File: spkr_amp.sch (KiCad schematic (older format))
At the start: 4 parts, among them U2 FSA2275UMX, U3 TPA2006D1DRBR

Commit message: Lots of schematic cleanup and board tweaking
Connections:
- wire segments 6 -> 11
- no-connect marks 1 -> 0
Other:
- moved on the sheet: C3, C7, U5
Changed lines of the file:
@@
 $Descr A4 11693 8268
 encoding utf-8
-Sheet 3 3
+Sheet 2 3
 Title ""
 Date ""
@@
 L TPA2006D1DRBR:TPA2006D1DRBR U?
 U 1 1 6026AF34
-P 5500 3300
+P 6900 3500
 AR Path="/6026AF34" Ref="U?"  Part="1"
 AR Path="/6026A3BE/6026AF34" Ref="U3"  Part="1"
 AR Path="/60276BEA/6026AF34" Ref="U5"  Part="1"
-F 0 "U5" H 6900 3687 60  0000 C CNN
-F 1 "TPA2006D1DRBR" H 6900 3581 60  0000 C CNN
-F 2 "footprints:TPA2006D1DRBR" H 6900 3540 60  0001 C CNN
-F 3 "" H 5500 3300 60  0000 C CNN
-	1    5500 3300
+F 0 "U5" H 6900 3550 60  0000 C CNN
+F 1 "TPA2006D1DRBR" H 6900 3450 60  0000 C CNN
+F 2 "footprints:TPA2006D1DRBR" H 8300 3740 60  0001 C CNN
+F 3 "" H 6900 3500 60  0000 C CNN
+	1    6900 3500
 	1    0    0    -1
 $EndComp
@@
 L power:GND #PWR06
 U 1 1 6027011E
-P 8300 3300
+P 6950 4150
 AR Path="/6026A3BE/6027011E" Ref="#PWR06"  Part="1"
 AR Path="/60276BEA/6027011E" Ref="#PWR011"  Part="1"
-F 0 "#PWR011" H 8300 3050 50  0001 C CNN
-F 1 "GND" V 8305 3172 50  0000 R CNN
-F 2 "" H 8300 3300 50  0001 C CNN
-F 3 "" H 8300 3300 50  0001 C CNN
-	1    8300 3300
-	0    -1   -1   0
+F 0 "#PWR011" H 6950 3900 50  0001 C CNN
+F 1 "GND" V 6955 4022 50  0000 R CNN
+F 2 "" H 6950 4150 50  0001 C CNN
+F 3 "" H 6950 4150 50  0001 C CNN
+	1    6950 4150
+	1    0    0    -1
 $EndComp
 $Comp
 L power:GND #PWR07
 U 1 1 60270A57
-P 8300 3500
+P 6850 4150
 AR Path="/6026A3BE/60270A57" Ref="#PWR07"  Part="1"
 AR Path="/60276BEA/60270A57" Ref="#PWR012"  Part="1"
-F 0 "#PWR012" H 8300 3250 50  0001 C CNN
-F 1 "GND" V 8305 3372 50  0000 R CNN
-F 2 "" H 8300 3500 50  0001 C CNN
-F 3 "" H 8300 3500 50  0001 C CNN
-	1    8300 3500
-	0    -1   -1   0
-$EndComp
-NoConn ~ 5500 3400
-Text HLabel 9050 3600 2    50   Input ~ 0
-VDD
-Text HLabel 8300 3400 2    50   Output ~ 0
-SPKR+
-Text HLabel 8300 3700 2    50   Output ~ 0
-SPKR-
-Text HLabel 3800 3150 1    50   Input ~ 0
-VDD
-$Comp
-L power:GND #PWR05
-U 1 1 6027124D
-P 3800 4150
-AR Path="/6026A3BE/6027124D" Ref="#PWR05"  Part="1"
-AR Path="/60276BEA/6027124D" Ref="#PWR010"  Part="1"
-F 0 "#PWR010" H 3800 3900 50  0001 C CNN
-F 1 "GND" H 3805 3977 50  0000 C CNN
-F 2 "" H 3800 4150 50  0001 C CNN
-F 3 "" H 3800 4150 50  0001 C CNN
-	1    3800 4150
+F 0 "#PWR012" H 6850 3900 50  0001 C CNN
+F 1 "GND" V 6855 4022 50  0000 R CNN
+F 2 "" H 6850 4150 50  0001 C CNN
+F 3 "" H 6850 4150 50  0001 C CNN
+	1    6850 4150
 	1    0    0    -1
 $EndComp
-$Comp
-L power:GND #PWR03
-U 1 1 6027187C
-P 3100 3500
-AR Path="/6026A3BE/6027187C" Ref="#PWR03"  Part="1"
-AR Path="/60276BEA/6027187C" Ref="#PWR08"  Part="1"
-F 0 "#PWR08" H 3100 3250 50  0001 C CNN
-F 1 "GND" V 3105 3372 50  0000 R CNN
-F 2 "" H 3100 3500 50  0001 C CNN
-F 3 "" H 3100 3500 50  0001 C CNN
-	1    3100 3500
-	0    1    1    0
-$EndComp
-Text HLabel 5500 3300 0    50   Input ~ 0
+Text HLabel 7650 2650 2    50   Input ~ 0
+VDD
+Text HLabel 8300 3450 2    50   Output ~ 0
+SPKR+
+Text HLabel 8300 3550 2    50   Output ~ 0
+SPKR-
+Text HLabel 3750 3150 1    50   Input ~ 0
+VDD
+Text HLabel 5500 3400 0    50   Input ~ 0
 ~SHUTDOWN
-Text HLabel 3100 3700 0    50   Input ~ 0
+Text HLabel 3100 3750 0    50   Input ~ 0
 LINEIN+
-Text HLabel 3100 3600 0    50   Input ~ 0
+Text HLabel 3100 3650 0    50   Input ~ 0
 LINEIN-
-Text HLabel 3100 3800 0    50   Input ~ 0
+Text HLabel 3100 3850 0    50   Input ~ 0
 SEL
 Text HLabel 4400 3800 2    50   Input ~ 0
@@
 Text HLabel 4400 3600 2    50   Input ~ 0
 LINEOUT-
-Text HLabel 3700 4150 3    50   Input ~ 0
+Text HLabel 3100 3550 0    50   Input ~ 0
 MUTE
 $Comp
 L Device:C C2
 U 1 1 60273CC0
-P 3550 2900
+P 2700 3450
 AR Path="/6026A3BE/60273CC0" Ref="C2"  Part="1"
 AR Path="/60276BEA/60273CC0" Ref="C3"  Part="1"
-F 0 "C3" V 3298 2900 50  0000 C CNN
-F 1 "0.1uF" V 3389 2900 50  0000 C CNN
-F 2 "Capacitor_SMD:C_0402_1005Metric" H 3588 2750 50  0001 C CNN
-F 3 "~" H 3550 2900 50  0001 C CNN
-	1    3550 2900
+F 0 "C3" V 2448 3450 50  0000 C CNN
+F 1 "0.1uF" V 2539 3450 50  0000 C CNN
+F 2 "Capacitor_SMD:C_0402_1005Metric" H 2738 3300 50  0001 C CNN
+F 3 "~" H 2700 3450 50  0001 C CNN
+	1    2700 3450
 	0    1    1    0
 $EndComp
-Wire Wire Line
-	3700 2900 3700 3150
 $Comp
 L power:GND #PWR04
 U 1 1 60274CA1
-P 3400 2900
+P 2550 3450
 AR Path="/6026A3BE/60274CA1" Ref="#PWR04"  Part="1"
 AR Path="/60276BEA/60274CA1" Ref="#PWR09"  Part="1"
-F 0 "#PWR09" H 3400 2650 50  0001 C CNN
-F 1 "GND" V 3405 2772 50  0000 R CNN
-F 2 "" H 3400 2900 50  0001 C CNN
-F 3 "" H 3400 2900 50  0001 C CNN
-	1    3400 2900
-	0    1    1    0
+F 0 "#PWR09" H 2550 3200 50  0001 C CNN
+F 1 "GND" V 2555 3322 50  0000 R CNN
+F 2 "" H 2550 3450 50  0001 C CNN
+F 3 "" H 2550 3450 50  0001 C CNN
+	1    2550 3450
+	1    0    0    -1
 $EndComp
 Text Label 5200 3500 0    50   ~ 0
@@
 L Device:C C7
 U 1 1 6034D245
-P 9050 3750
+P 7650 2800
 AR Path="/60276BEA/6034D245" Ref="C7"  Part="1"
 AR Path="/6026A3BE/6034D245" Ref="C6"  Part="1"
-F 0 "C7" H 9165 3796 50  0000 L CNN
-F 1 "1uF" H 9165 3705 50  0000 L CNN
-F 2 "Capacitor_SMD:C_0402_1005Metric" H 9088 3600 50  0001 C CNN
-F 3 "~" H 9050 3750 50  0001 C CNN
-	1    9050 3750
+F 0 "C7" H 7765 2846 50  0000 L CNN
+F 1 "1uF" H 7765 2755 50  0000 L CNN
+F 2 "Capacitor_SMD:C_0402_1005Metric" H 7688 2650 50  0001 C CNN
+F 3 "~" H 7650 2800 50  0001 C CNN
+	1    7650 2800
 	1    0    0    -1
 $EndComp
 Wire Wire Line
-	8300 3600 9050 3600
+	6900 2650 7650 2650
 $Comp
 L power:GND #PWR0105
 U 1 1 6034E328
-P 9050 3900
+P 7650 2950
 AR Path="/60276BEA/6034E328" Ref="#PWR0105"  Part="1"
 AR Path="/6026A3BE/6034E328" Ref="#PWR0104"  Part="1"
-F 0 "#PWR0105" H 9050 3650 50  0001 C CNN
-F 1 "GND" H 9055 3727 50  0000 C CNN
-F 2 "" H 9050 3900 50  0001 C CNN
-F 3 "" H 9050 3900 50  0001 C CNN
-	1    9050 3900
+F 0 "#PWR0105" H 7650 2700 50  0001 C CNN
+F 1 "GND" H 7655 2777 50  0000 C CNN
+F 2 "" H 7650 2950 50  0001 C CNN
+F 3 "" H 7650 2950 50  0001 C CNN
+	1    7650 2950
 	1    0    0    -1
 $EndComp
+Wire Wire Line
+	6900 2650 6900 2850
+$Comp
+L power:GND #PWR0107
+U 1 1 6043B2A1
+P 3750 4250
+AR Path="/6026A3BE/6043B2A1" Ref="#PWR0107"  Part="1"
+AR Path="/60276BEA/6043B2A1" Ref="#PWR0108"  Part="1"
+F 0 "#PWR0108" H 3750 4000 50  0001 C CNN
+F 1 "GND" H 3755 4077 50  0000 C CNN
+F 2 "" H 3750 4250 50  0001 C CNN
+F 3 "" H 3750 4250 50  0001 C CNN
+	1    3750 4250
+	1    0    0    -1
+$EndComp
+Wire Wire Line
+	3800 4150 3800 4250
+Wire Wire Line
+	3800 4250 3750 4250
+Wire Wire Line
+	3700 4250 3700 4150
+Connection ~ 3750 4250
+Wire Wire Line
+	3750 4250 3700 4250
+Wire Wire Line
+	2850 3450 3100 3450
 $EndSCHEMATC

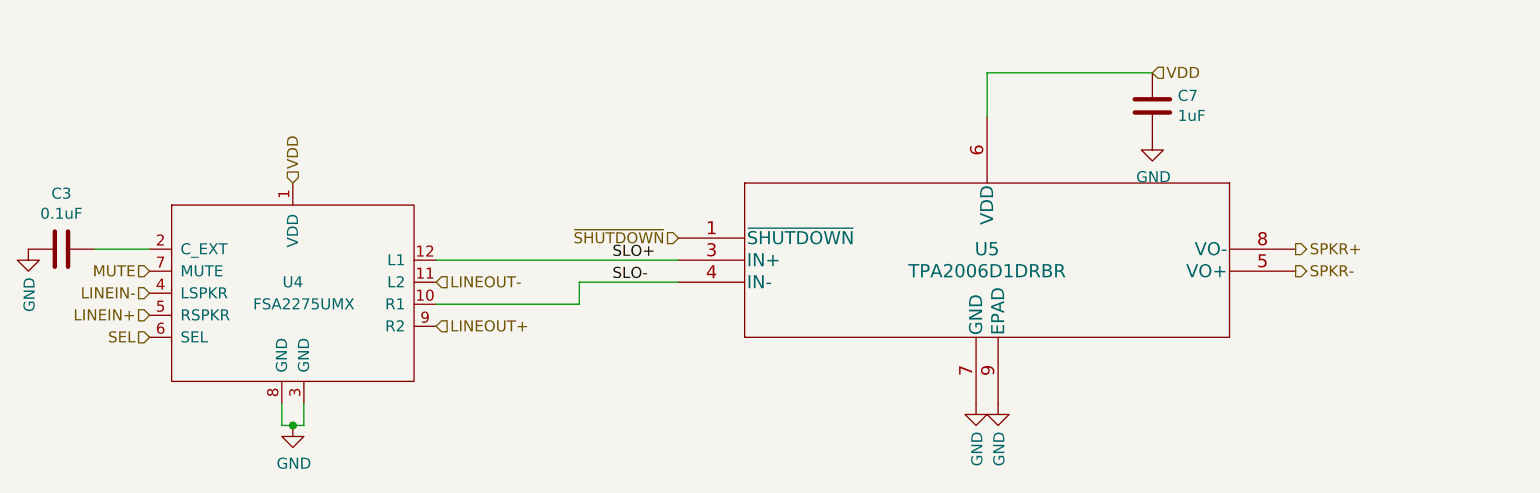
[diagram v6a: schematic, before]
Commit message: AC-couple headphone outputs. This frees up HPRCOM and HPLCOM, which I can use for line outputs, since the dock line out is single-ended anyway.
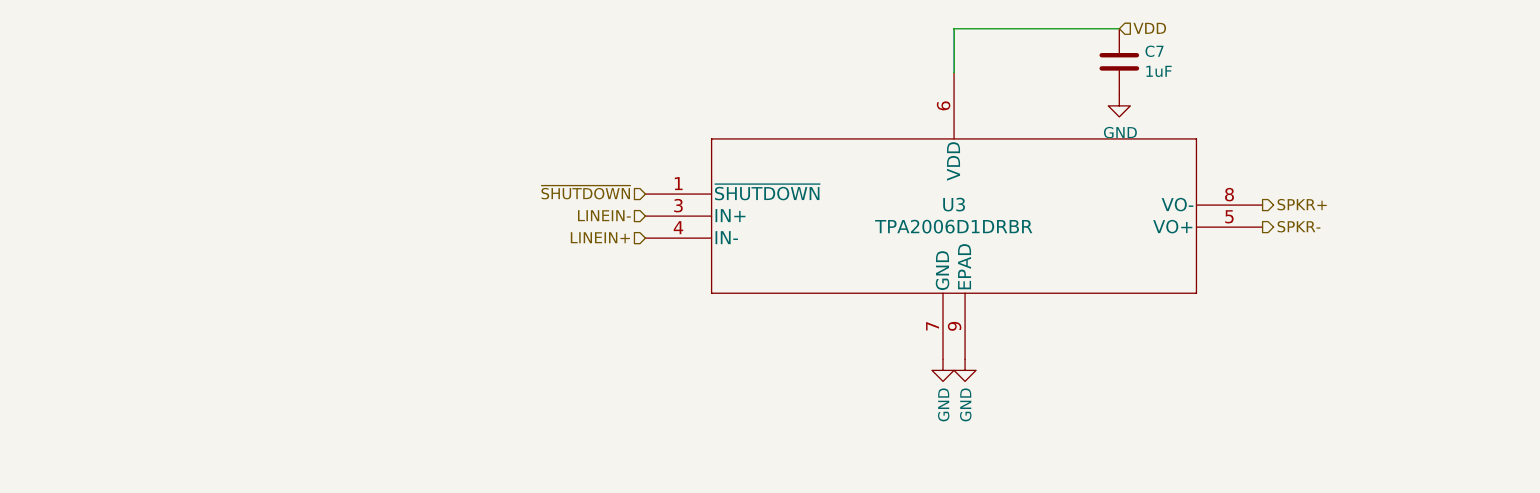
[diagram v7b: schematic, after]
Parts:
- removed C2: 0.1uF, Capacitor_SMD:C_0402_1005Metric, symbol Device:C
- removed U2: FSA2275UMX, footprints:FSA2275, symbol FSA2275UMX:FSA2275UMX
- removed U3: TPA2006D1DRBR, footprints:TPA2006D1DRBR, symbol TPA2006D1DRBR:TPA2006D1DRBR
- added U2: TPA2006D1DRBR, footprints:TPA2006D1DRBR, symbol TPA2006D1DRBR:TPA2006D1DRBR
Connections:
- net GND: now also U2.7 (GND), U2.9 (EPAD)
- net LINEIN+: now also U2.4 (IN-)
- net LINEIN-: now also U2.3 (IN+)
- net SPKR+: now also U2.8 (VO-)
- net SPKR-: now also U2.5 (VO+)
- net VDD: now also U2.6 (VDD)
- net ~SHUTDOWN: now also U2.1 (~SHUTDOWN)
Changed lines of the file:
@@
 $Descr A4 11693 8268
 encoding utf-8
-Sheet 2 3
+Sheet 3 3
 Title ""
 Date ""
@@
 Comment4 ""
 $EndDescr
+Wire Wire Line
+	6750 2450 6750 2650
 $Comp
-L TPA2006D1DRBR:TPA2006D1DRBR U?
-U 1 1 6026AF34
-P 6900 3500
-AR Path="/6026AF34" Ref="U?"  Part="1"
-AR Path="/6026A3BE/6026AF34" Ref="U3"  Part="1"
-AR Path="/60276BEA/6026AF34" Ref="U5"  Part="1"
-F 0 "U5" H 6900 3550 60  0000 C CNN
-F 1 "TPA2006D1DRBR" H 6900 3450 60  0000 C CNN
-F 2 "footprints:TPA2006D1DRBR" H 8300 3740 60  0001 C CNN
-F 3 "" H 6900 3500 60  0000 C CNN
-	1    6900 3500
+L power:GND #PWR010
+U 1 1 603FDDB9
+P 7500 2750
+AR Path="/60276BEA/603FDDB9" Ref="#PWR010"  Part="1"
+AR Path="/6026A3BE/603FDDB9" Ref="#PWR07"  Part="1"
+F 0 "#PWR010" H 7500 2500 50  0001 C CNN
+F 1 "GND" H 7505 2577 50  0000 C CNN
+F 2 "" H 7500 2750 50  0001 C CNN
+F 3 "" H 7500 2750 50  0001 C CNN
+	1    7500 2750
+	1    0    0    -1
+$EndComp
+Wire Wire Line
+	6750 2450 7500 2450
+$Comp
+L Device:C C7
+U 1 1 603FDDC0
+P 7500 2600
+AR Path="/60276BEA/603FDDC0" Ref="C7"  Part="1"
+AR Path="/6026A3BE/603FDDC0" Ref="C6"  Part="1"
+F 0 "C7" H 7615 2646 50  0000 L CNN
+F 1 "1uF" H 7615 2555 50  0000 L CNN
+F 2 "Capacitor_SMD:C_0402_1005Metric" H 7538 2450 50  0001 C CNN
+F 3 "~" H 7500 2600 50  0001 C CNN
+	1    7500 2600
+	1    0    0    -1
+$EndComp
+Text HLabel 5350 3300 0    50   Input ~ 0
+LINEIN-
+Text HLabel 5350 3400 0    50   Input ~ 0
+LINEIN+
+Text HLabel 5350 3200 0    50   Input ~ 0
+~SHUTDOWN
+Text HLabel 8150 3350 2    50   Output ~ 0
+SPKR-
+Text HLabel 8150 3250 2    50   Output ~ 0
+SPKR+
+Text HLabel 7500 2450 2    50   Input ~ 0
+VDD
+$Comp
+L power:GND #PWR05
+U 1 1 603FDDCC
+P 6700 3950
+AR Path="/6026A3BE/603FDDCC" Ref="#PWR05"  Part="1"
+AR Path="/60276BEA/603FDDCC" Ref="#PWR08"  Part="1"
+F 0 "#PWR08" H 6700 3700 50  0001 C CNN
+F 1 "GND" V 6705 3822 50  0000 R CNN
+F 2 "" H 6700 3950 50  0001 C CNN
+F 3 "" H 6700 3950 50  0001 C CNN
+	1    6700 3950
 	1    0    0    -1
 $EndComp
 $Comp
 L power:GND #PWR06
-U 1 1 6027011E
-P 6950 4150
-AR Path="/6026A3BE/6027011E" Ref="#PWR06"  Part="1"
-AR Path="/60276BEA/6027011E" Ref="#PWR011"  Part="1"
-F 0 "#PWR011" H 6950 3900 50  0001 C CNN
-F 1 "GND" V 6955 4022 50  0000 R CNN
-F 2 "" H 6950 4150 50  0001 C CNN
-F 3 "" H 6950 4150 50  0001 C CNN
-	1    6950 4150
+U 1 1 603FDDD2
+P 6800 3950
+AR Path="/6026A3BE/603FDDD2" Ref="#PWR06"  Part="1"
+AR Path="/60276BEA/603FDDD2" Ref="#PWR09"  Part="1"
+F 0 "#PWR09" H 6800 3700 50  0001 C CNN
+F 1 "GND" V 6805 3822 50  0000 R CNN
+F 2 "" H 6800 3950 50  0001 C CNN
+F 3 "" H 6800 3950 50  0001 C CNN
+	1    6800 3950
 	1    0    0    -1
 $EndComp
 $Comp
-L power:GND #PWR07
-U 1 1 60270A57
-P 6850 4150
-AR Path="/6026A3BE/60270A57" Ref="#PWR07"  Part="1"
-AR Path="/60276BEA/60270A57" Ref="#PWR012"  Part="1"
-F 0 "#PWR012" H 6850 3900 50  0001 C CNN
-F 1 "GND" V 6855 4022 50  0000 R CNN
-F 2 "" H 6850 4150 50  0001 C CNN
-F 3 "" H 6850 4150 50  0001 C CNN
-	1    6850 4150
+L TPA2006D1DRBR:TPA2006D1DRBR U?
+U 1 1 603FDDD8
+P 6750 3300
+AR Path="/603FDDD8" Ref="U?"  Part="1"
+AR Path="/6026A3BE/603FDDD8" Ref="U2"  Part="1"
+AR Path="/60276BEA/603FDDD8" Ref="U3"  Part="1"
+F 0 "U3" H 6750 3350 60  0000 C CNN
+F 1 "TPA2006D1DRBR" H 6750 3250 60  0000 C CNN
+F 2 "footprints:TPA2006D1DRBR" H 8150 3540 60  0001 C CNN
+F 3 "" H 6750 3300 60  0000 C CNN
+	1    6750 3300
 	1    0    0    -1
 $EndComp
-Text HLabel 7650 2650 2    50   Input ~ 0
-VDD
-Text HLabel 8300 3450 2    50   Output ~ 0
-SPKR+
-Text HLabel 8300 3550 2    50   Output ~ 0
-SPKR-
-Text HLabel 3750 3150 1    50   Input ~ 0
-VDD
-Text HLabel 5500 3400 0    50   Input ~ 0
-~SHUTDOWN
-Text HLabel 3100 3750 0    50   Input ~ 0
-LINEIN+
-Text HLabel 3100 3650 0    50   Input ~ 0
-LINEIN-
-Text HLabel 3100 3850 0    50   Input ~ 0
-SEL
-Text HLabel 4400 3800 2    50   Input ~ 0
-LINEOUT+
-Text HLabel 4400 3600 2    50   Input ~ 0
-LINEOUT-
-Text HLabel 3100 3550 0    50   Input ~ 0
-MUTE
-$Comp
-L Device:C C2
-U 1 1 60273CC0
-P 2700 3450
-AR Path="/6026A3BE/60273CC0" Ref="C2"  Part="1"
-AR Path="/60276BEA/60273CC0" Ref="C3"  Part="1"
-F 0 "C3" V 2448 3450 50  0000 C CNN
-F 1 "0.1uF" V 2539 3450 50  0000 C CNN
-F 2 "Capacitor_SMD:C_0402_1005Metric" H 2738 3300 50  0001 C CNN
-F 3 "~" H 2700 3450 50  0001 C CNN
-	1    2700 3450
-	0    1    1    0
-$EndComp
-$Comp
-L power:GND #PWR04
-U 1 1 60274CA1
-P 2550 3450
-AR Path="/6026A3BE/60274CA1" Ref="#PWR04"  Part="1"
-AR Path="/60276BEA/60274CA1" Ref="#PWR09"  Part="1"
-F 0 "#PWR09" H 2550 3200 50  0001 C CNN
-F 1 "GND" V 2555 3322 50  0000 R CNN
-F 2 "" H 2550 3450 50  0001 C CNN
-F 3 "" H 2550 3450 50  0001 C CNN
-	1    2550 3450
-	1    0    0    -1
-$EndComp
-Text Label 5200 3500 0    50   ~ 0
-SLO+
-$Comp
-L FSA2275UMX:FSA2275UMX U?
-U 1 1 6026AF3A
-P 3750 3650
-AR Path="/6026AF3A" Ref="U?"  Part="1"
-AR Path="/6026A3BE/6026AF3A" Ref="U2"  Part="1"
-AR Path="/60276BEA/6026AF3A" Ref="U4"  Part="1"
-F 0 "U4" H 3750 3700 50  0000 C CNN
-F 1 "FSA2275UMX" H 3800 3600 50  0000 C CNN
-F 2 "footprints:FSA2275" H 3750 3650 50  0001 C CNN
-F 3 "" H 3750 3650 50  0001 C CNN
-	1    3750 3650
-	1    0    0    -1
-$EndComp
-Wire Wire Line
-	4400 3500 5500 3500
-Wire Wire Line
-	5500 3600 5050 3600
-Wire Wire Line
-	5050 3600 5050 3700
-Wire Wire Line
-	5050 3700 4400 3700
-Text Label 5200 3600 0    50   ~ 0
-SLO-
-$Comp
-L Device:C C7
-U 1 1 6034D245
-P 7650 2800
-AR Path="/60276BEA/6034D245" Ref="C7"  Part="1"
-AR Path="/6026A3BE/6034D245" Ref="C6"  Part="1"
-F 0 "C7" H 7765 2846 50  0000 L CNN
-F 1 "1uF" H 7765 2755 50  0000 L CNN
-F 2 "Capacitor_SMD:C_0402_1005Metric" H 7688 2650 50  0001 C CNN
-F 3 "~" H 7650 2800 50  0001 C CNN
-	1    7650 2800
-	1    0    0    -1
-$EndComp
-Wire Wire Line
-	6900 2650 7650 2650
-$Comp
-L power:GND #PWR0105
-U 1 1 6034E328
-P 7650 2950
-AR Path="/60276BEA/6034E328" Ref="#PWR0105"  Part="1"
-AR Path="/6026A3BE/6034E328" Ref="#PWR0104"  Part="1"
-F 0 "#PWR0105" H 7650 2700 50  0001 C CNN
-F 1 "GND" H 7655 2777 50  0000 C CNN
-F 2 "" H 7650 2950 50  0001 C CNN
-F 3 "" H 7650 2950 50  0001 C CNN
-	1    7650 2950
-	1    0    0    -1
-$EndComp
-Wire Wire Line
-	6900 2650 6900 2850
-$Comp
-L power:GND #PWR0107
-U 1 1 6043B2A1
-P 3750 4250
-AR Path="/6026A3BE/6043B2A1" Ref="#PWR0107"  Part="1"
-AR Path="/60276BEA/6043B2A1" Ref="#PWR0108"  Part="1"
-F 0 "#PWR0108" H 3750 4000 50  0001 C CNN
-F 1 "GND" H 3755 4077 50  0000 C CNN
-F 2 "" H 3750 4250 50  0001 C CNN
-F 3 "" H 3750 4250 50  0001 C CNN
-	1    3750 4250
-	1    0    0    -1
-$EndComp
-Wire Wire Line
-	3800 4150 3800 4250
-Wire Wire Line
-	3800 4250 3750 4250
-Wire Wire Line
-	3700 4250 3700 4150
-Connection ~ 3750 4250
-Wire Wire Line
-	3750 4250 3700 4250
-Wire Wire Line
-	2850 3450 3100 3450
 $EndSCHEMATC
